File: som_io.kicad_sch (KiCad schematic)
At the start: 59 parts, among them J1 Hermaphroditic_Molex_203456-0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, J20 Tag-Connect_TC2050-IDC-NL_2x5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, Q28 PJE138K, U1 NTS0102_XSON, U2 NTS0102_XSON, U3 NTS0102_XSON, U39 NTS0102_XSON, U4 NTS0102_XSON, U5 NTS0102_XSON, U59 TXU0304BQAR, U60 TXS0104E_VQFN, U61 TXS0104E_VQFN, U62 TXS0104E_VQFN, U63 TXS0104E_VQFN, U64 TXS0104E_VQFN, U65 NTS0102_XSON, U66 NTS0102_XSON, U67 NTS0102_XSON, U68 NTS0102_XSON

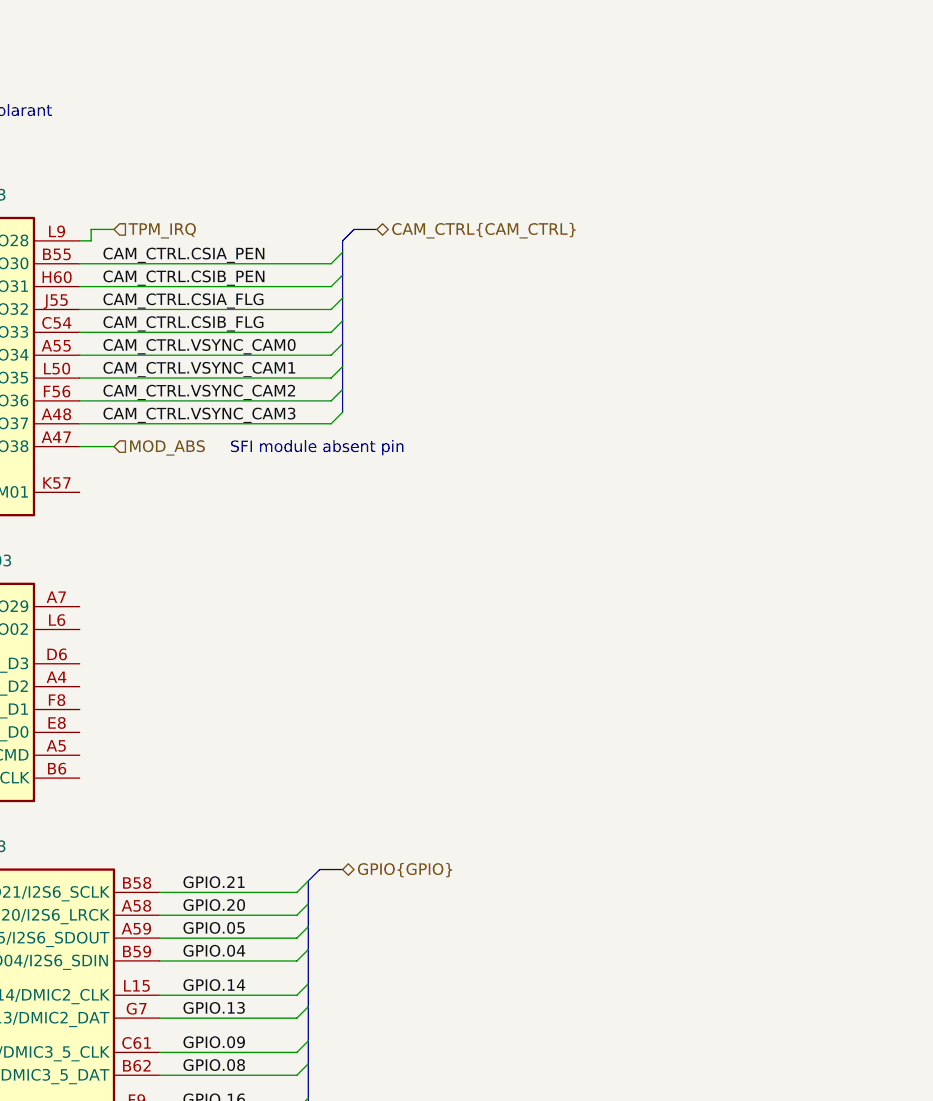
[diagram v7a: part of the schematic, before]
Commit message: [#82837] Finish mapping interfaces, waiting for new SoM symbol
[#82837] Add GPIO level shifter and route USB related GPIO on root
schematic

[#82837] WIP: Modify Power-up and reset section
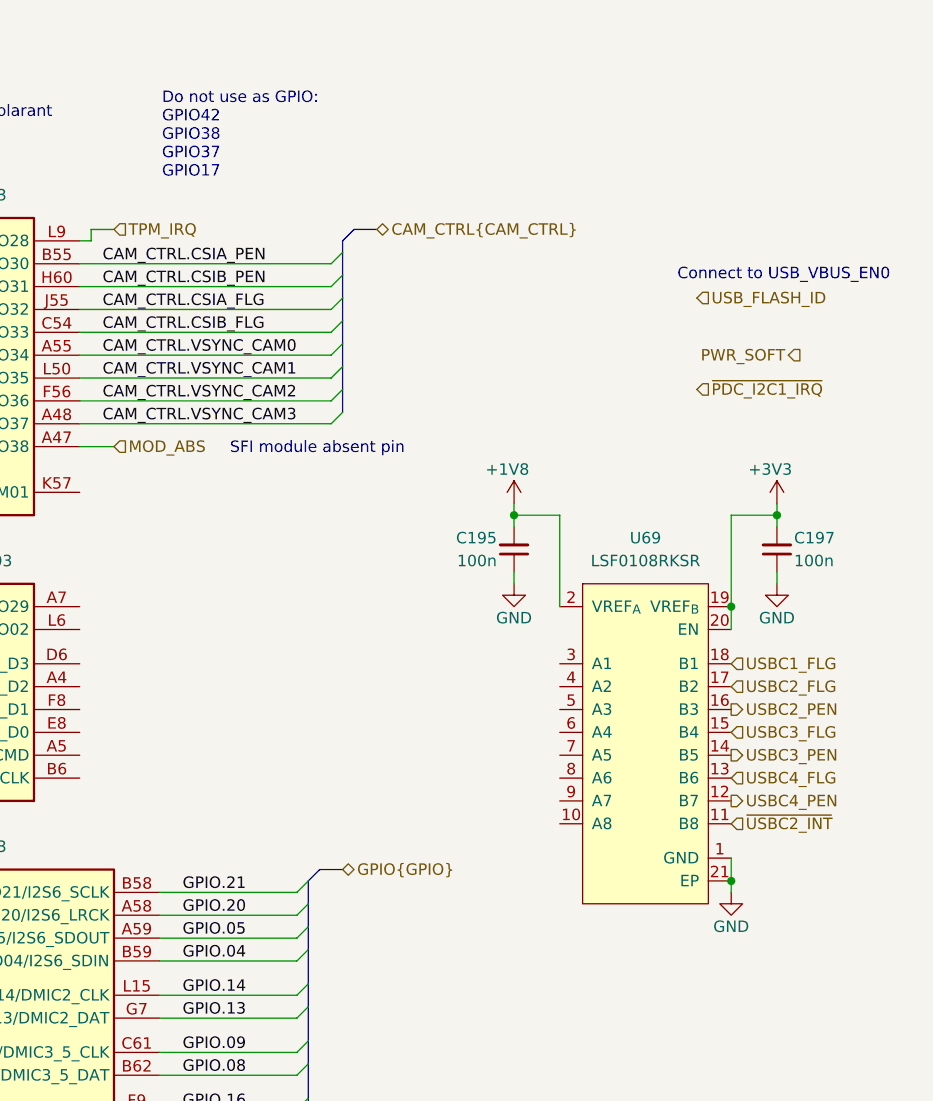
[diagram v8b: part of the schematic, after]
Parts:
- added C195, C197: C_100n_0402, antmicro-footprints:C_0402_1005Metric, symbol antmicroCapacitors0402:C_100n_0402
- added U69: LSF0108RKSR, antmicro-footprints:VQFN-20_1EP_4.5x2.5mm_P0.5mm, symbol antmicroLogicTranslatorsLevelShifters:LSF0108RKSR
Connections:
- net +1V8: now also C195.2, U69.2 (VREF_{A})
- net +3V3: now also C197.2, U69.19 (VREF_{B}), U69.20 (EN)
- net GND: now also C195.1, C197.1, U69.1 (GND), U69.21 (EP)
- new net USBC1_FLG: U69.18 (B1)
- new net USBC2_FLG: U69.17 (B2)
- new net USBC2_PEN: U69.16 (B3)
- new net USBC3_FLG: U69.15 (B4)
- new net USBC3_PEN: U69.14 (B5)
- new net USBC4_FLG: U69.13 (B6)
- new net USBC4_PEN: U69.12 (B7)
- new net ~{USBC2_INT}: U69.11 (B8)
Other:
- note added: "Connect to USB_VBUS_EN0"
- note added: "Do not use as GPIO: GPIO42 GPIO38 GPIO37 GPIO17"
